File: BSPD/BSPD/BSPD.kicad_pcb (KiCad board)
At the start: 2 copper layers, 44 x 36 mm, 55 parts, among them J1 430450613, K1 AZ943-1CH-12DE, U3 74HC1G08GW_125, U4 74HC1G02GW_125, U5 LTC6994CS6-1-TRMPBF, U6 DRDC3105F-7, U7 LD1117S50TR_SOT223, U9 74HC32D_653

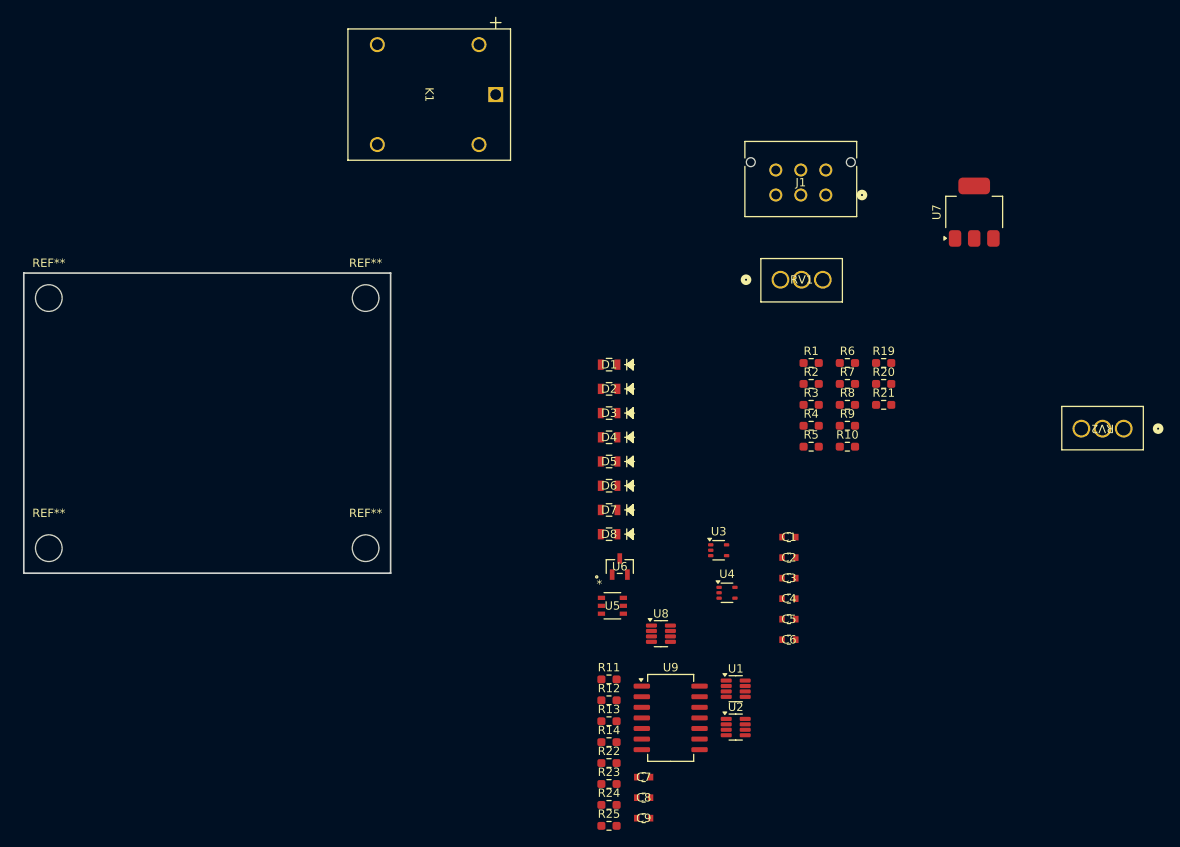
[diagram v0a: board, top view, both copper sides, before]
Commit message: Layout started and component changes
The footprints have all be chosen and the linear regulator was swapped out.
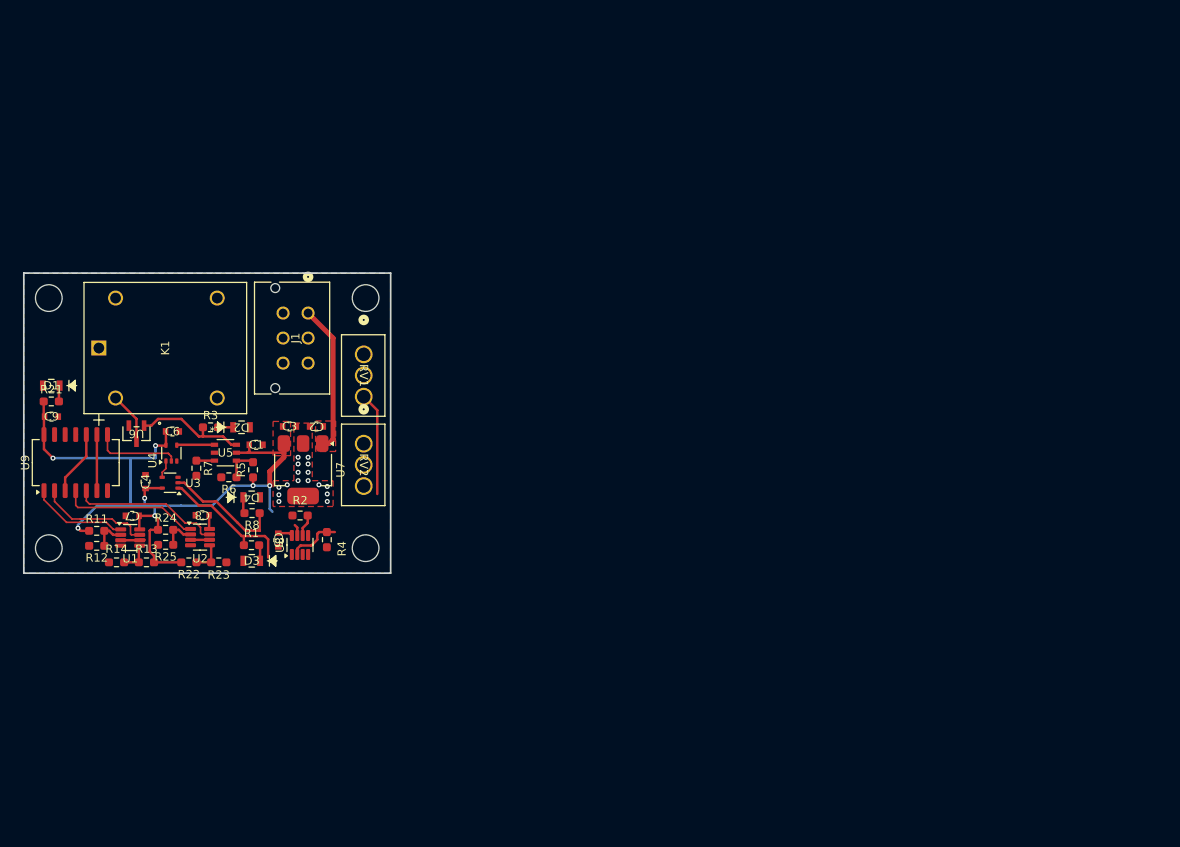
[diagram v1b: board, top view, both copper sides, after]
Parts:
- removed D5, D6, D7, D8: LED, CMD17_21VGD:LED0805N_CML
- removed R10, R19, R20, R9: 300, Resistor_SMD:R_0603_1608Metric_Pad0.98x0.95mm_HandSolder
- C2: value 100n -> 0.33u
- C3: value 10u -> 0.1u
- U7: value LD1117S50TR_SOT223 -> UA78M05CDCYR
- moved R21 99.8 mm to (54.3, 74.4)
- moved RV2 91.2 mm to (91.8, 79.5), turned to -90 degrees
- moved U7 86.2 mm to (84.5, 82.6), turned to -90 degrees
- moved C9 85.8 mm to (54.3, 76.2)
- moved R7 78.7 mm to (71.7, 82.4), turned to -90 degrees
- moved C4 78.4 mm to (65.6, 84.0), turned to 90 degrees
- moved C6 78.0 mm to (68.8, 78.0)
- moved U9 77.7 mm to (57.2, 81.7), turned to 90 degrees
- moved R6 75.4 mm to (75.6, 83.5), turned to 180 degrees
- moved U1 74.9 mm to (63.8, 90.7)
- moved R8 72.6 mm to (78.4, 87.8), turned to 180 degrees
- moved R3 72.1 mm to (73.4, 77.5)
- moved R1 70.6 mm to (78.3, 91.6)
- moved C7 68.9 mm to (64.0, 88.1), turned to 180 degrees
- moved U4 68.7 mm to (68.7, 80.6), turned to 90 degrees
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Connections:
- J1 pad 2: /Brake Sense -> Brake Sense
- J1 pad 3: /Current Sense -> Current Sense
- U1 pad 3: /FaultDetection/Brake Sense -> Brake Sense
- U1 pad 6: /FaultDetection/Brake Sense -> Brake Sense
- U2 pad 3: /FaultDetection/Current Sense -> Current Sense
- U2 pad 6: /FaultDetection/Current Sense -> Current Sense
- U4 pad 1: /Circuit Fault -> /BSP
- U4 pad 2: /BSP -> Circuit Fault
- U7 pad 1: GND -> +12V
- U7 pad 2: +5V -> GND
- U7 pad 3: +12V -> +5V
- U8 pad 3: /Brake Sense -> Brake Sense
- U8 pad 5: /Current Sense -> Current Sense
- U9 pad 10: Net-(U9-2Y) -> Net-(U9-1Y)
- U9 pad 8: /FaultDetection/Circuit Fault -> Circuit Fault
- U9 pad 9: Net-(U9-1Y) -> Net-(U9-2Y)
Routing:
- net +5V: track 0.00 -> 95.7 mm, vias 0 -> 7
- net Net-(U8-INA-): track 0.00 -> 18.8 mm
- net /FaultDetection/Current Under: track 0.00 -> 18.1 mm
- net +12V: track 0.00 -> 17.9 mm
- net /FaultDetection/Current Over: track 0.00 -> 16.8 mm
- net /Brake Applied: track 0.00 -> 16.6 mm
- net /Current Applied: track 0.00 -> 15.7 mm
- net /Relay Sig: track 0.00 -> 13.8 mm
- net /FaultDetection/Brake Under: track 0.00 -> 13.7 mm
- net /FaultDetection/Brake Over: track 0.00 -> 11.8 mm
- net Circuit Fault: track 0.00 -> 10.4 mm
- net Net-(U9-1Y): track 0.00 -> 7.78 mm
- net Net-(U9-2Y): track 0.00 -> 6.72 mm
- net Net-(U6-OUT): track 0.00 -> 6.32 mm
- net Net-(U4-Y): track 0.00 -> 4.54 mm
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- added copper zone on F.Cu, net +12V
- added copper zone on F.Cu, net +5V
- added copper zone on B.Cu, net GND
- added copper zone on F.Cu, net GND

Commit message: Update
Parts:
- moved RV2 39.6 mm to (53.8, 68.3), turned to 0 degrees
- moved R4 36.4 mm to (53.3, 78.0), turned to 180 degrees
- moved RV1 35.4 mm to (58.9, 81.8), turned to 180 degrees
- moved R21 35.2 mm to (86.5, 60.1), turned to 180 degrees
- moved R2 34.2 mm to (53.9, 72.0)
- moved U8 33.9 mm to (54.6, 75.0)
- moved C5 33.9 mm to (52.0, 74.4)
- moved D1 31.1 mm to (82.8, 60.1)
- moved K1 26.8 mm to (86.6, 70.7), turned to 0 degrees
- moved R13 22.5 mm to (69.1, 71.5)
- moved R22 22.3 mm to (76.7, 72.2), turned to 180 degrees
- moved R14 21.7 mm to (69.1, 73.2)
- moved R23 19.9 mm to (76.7, 73.9), turned to 180 degrees
- moved C8 18.4 mm to (70.2, 69.8)
- moved C7 18.3 mm to (63.7, 69.8)
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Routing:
- net GND: track 0.00 -> 70.8 mm, vias 16 -> 15
- net Current Sense: track 2.28 -> 41.7 mm, vias 0 -> 1
- net Brake Sense: track 2.90 -> 34.6 mm, vias 0 -> 2
- net /Shutdown Out: track 0.00 -> 29.5 mm
- net +5V: track 95.7 -> 123.7 mm, vias 7 -> 6
- net /Shutdown In: track 0.00 -> 15.8 mm
- net +12V: track 17.9 -> 32.9 mm
- net Net-(U8-INA-): track 18.8 -> 5.84 mm
- net Net-(U6-OUT): track 6.32 -> 17.1 mm
- net /Brake Applied: track 16.6 -> 26.6 mm, vias 0 -> 2
- net /Current Applied: track 15.7 -> 24.4 mm, vias 0 -> 2
- net Net-(U4-Y): track 4.54 -> 13.3 mm, vias 0 -> 2
- net /FaultDetection/Brake Over: track 11.8 -> 18.5 mm, vias 0 -> 2
- net /FaultDetection/Current Over: track 16.8 -> 10.9 mm
- net /FaultDetection/Current Under: track 18.1 -> 12.5 mm
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- removed copper zone on F.Cu, net +12V
- removed copper zone on F.Cu, net +5V
